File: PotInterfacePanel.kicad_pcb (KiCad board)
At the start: 2 copper layers, 168.1 x 33.4 mm, 29 parts, among them J5 Led, J6 Conn_01x02_Socket, J7 Conn_02x05_Odd_Even, Q1 BC547, Q2 BC547, U1 SM420561N, U2 ATmega328P-P, U4 SM420561N, Y1 Crystal

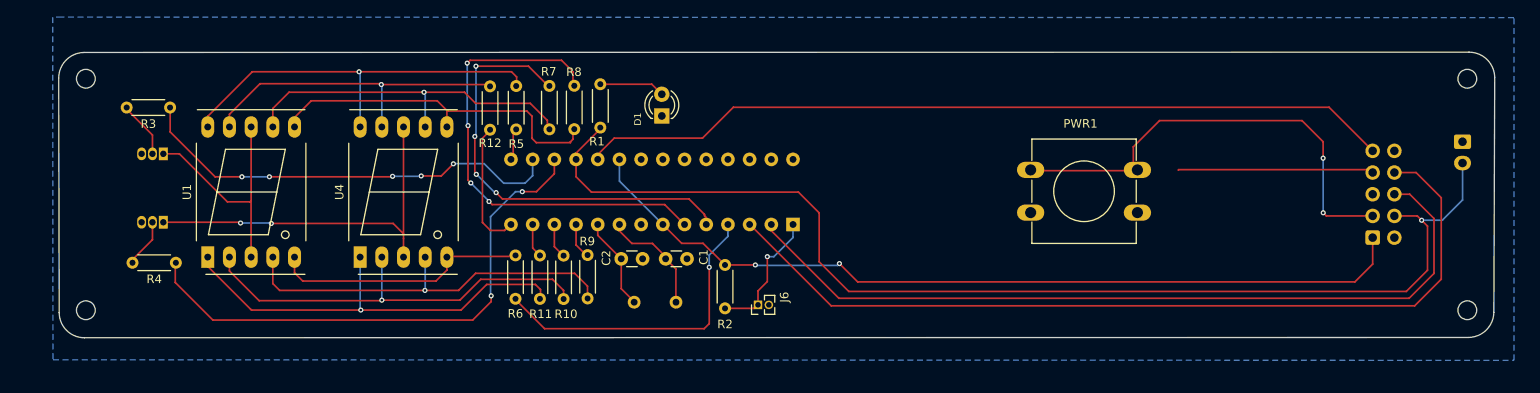
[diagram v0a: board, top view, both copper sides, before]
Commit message: 14seg-Display with a Potentiometer Knob
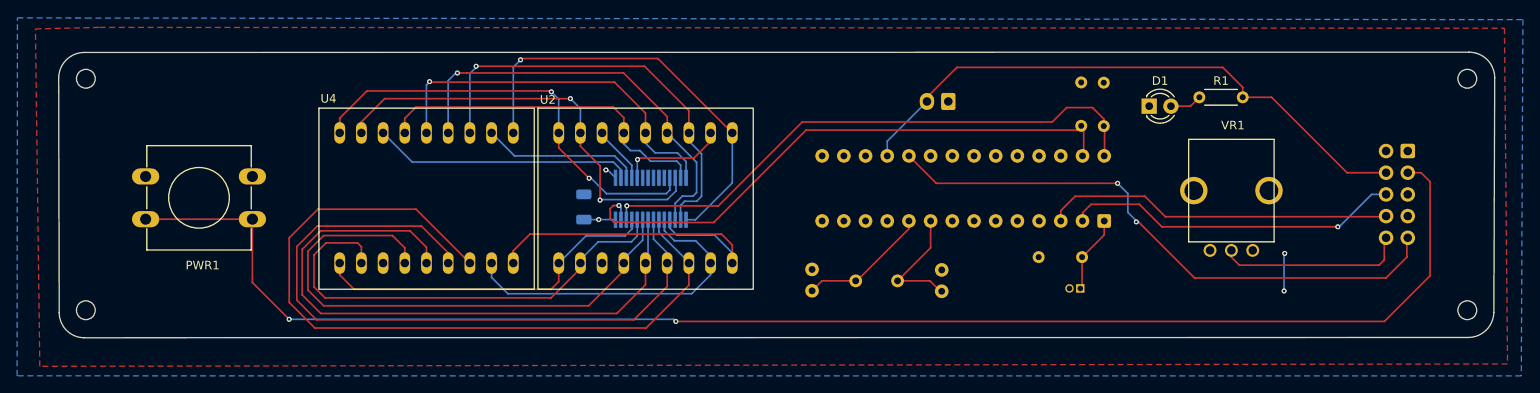
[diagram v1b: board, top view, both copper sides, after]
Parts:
- removed J5: Led, Connector_JST:JST_EH_B2B-EH-A_1x02_P2.50mm_Vertical
- removed J6: Conn_01x02_Socket, Connector_PinHeader_1.27mm:PinHeader_1x02_P1.27mm_Vertical
- removed J7: Conn_02x05_Odd_Even, Connector_IDC:IDC-Header_2x05_P2.54mm_Vertical
- removed Q1, Q2: BC547, Package_TO_SOT_THT:TO-92_Inline
- removed R10, R11, R4, R5, R6, R7, R8, R9: R, Resistor_THT:R_Axial_DIN0204_L3.6mm_D1.6mm_P5.08mm_Horizontal
- added C3: C, Capacitor_SMD:C_1206_3216Metric, B.Cu at (136.3, 95.0)
- added J1: Led, Connector_JST:JST_EH_B2B-EH-A_1x02_P2.50mm_Vertical, B.Cu at (179.0, 82.6)
- added J2: Conn_02x05_Odd_Even, Connector_IDC:IDC-Header_2x05_P2.54mm_Vertical, B.Cu at (232.8, 88.4)
- added J3: Conn_01x02_Socket, Connector_PinHeader_1.27mm:PinHeader_1x02_P1.27mm_Vertical, B.Cu at (194.5, 104.5)
- added U3: ATmega328P-P, Package_DIP:DIP-28_W7.62mm, B.Cu at (197.3, 96.6)
- added VR1: PTV09A-4225F-B104, pot:PTV09, F.Cu at (212.2, 100.1)
- C1, C2: moved to B.Cu
- R12: value R -> 10k; moved to B.Cu
- R2: value 10k -> 4.7k; moved to B.Cu
- R3: value R -> 4.7k; moved to B.Cu
- U1: value SM420561N -> HT16K33A-28SSOP; footprint Display_7Segment:7SegmentLED_LTS6760_LTS6780 -> ht16k33A-28ssop:SOP63P600X175-28N; moved to B.Cu
- U2: value ATmega328P-P -> ~; footprint Package_DIP:DIP-28_W7.62mm -> custom_footprint:14seg; moved to F.Cu
- U4: value SM420561N -> ~; footprint Display_7Segment:7SegmentLED_LTS6760_LTS6780 -> custom_footprint:14seg
- moved R3 106.7 mm to (194.6, 85.5), turned to 90 degrees
- moved PWR1 91.3 mm to (97.5, 96.4), turned to 180 degrees
- moved R1 70.1 mm to (208.4, 82.1), turned to 0 degrees
- moved R12 65.9 mm to (189.6, 100.8), turned to 0 degrees
- moved D1 57.1 mm to (202.5, 83.2), turned to 0 degrees
- moved U1 52.3 mm to (144.2, 94.0), turned to -90 degrees
- moved R2 47.2 mm to (197.2, 85.5), turned to 90 degrees
- moved U2 32.8 mm to (131.0, 83.4), turned to 0 degrees
- moved C1 32.5 mm to (178.2, 104.8), turned to 90 degrees
- moved Y1 26.1 mm to (168.2, 103.6)
- moved C2 22.7 mm to (163.1, 104.8), turned to 90 degrees
- moved U4 18.1 mm to (105.3, 83.4), turned to 0 degrees
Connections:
- C1 pad 1: (no net) -> Net-(U3-XTAL1/PB6)
- C2 pad 1: (no net) -> Net-(U3-XTAL2/PB7)
- D1 pad 2: (no net) -> Net-(D1-A)
- R1 pad 1: (no net) -> Net-(D1-A)
- R12 pad 1: (no net) -> 5V
- R12 pad 2: F -> Net-(J3-Pin_1)
- R2 pad 1: 5V -> /SCL
- R2 pad 2: (no net) -> 5V
- R3 pad 1: (no net) -> /SDA
- R3 pad 2: CC1 -> 5V
- U1 pad 1: E -> GND
- U1 pad 10: G -> unconnected-(U1-ROW15/K13/INT-Pad10)
- U1 pad 2: D -> DG4
- U1 pad 3: (no net) -> DG3
- U1 pad 4: C -> DG2
- U1 pad 5: DPX -> DG1
- U1 pad 6: B -> unconnected-(U1-COM4-Pad6)
- U1 pad 7: A -> unconnected-(U1-COM5-Pad7)
- U1 pad 8: (no net) -> unconnected-(U1-COM6-Pad8)
- U1 pad 9: F -> unconnected-(U1-COM7-Pad9)
- U2 pad 1: (no net) -> e
- U2 pad 10: (no net) -> b
- U2 pad 11: (no net) -> DG1
- U2 pad 12: (no net) -> 1
- U2 pad 13: (no net) -> p
- U2 pad 14: (no net) -> j
- U2 pad 15: (no net) -> h
- U2 pad 16: (no net) -> DG2
- U2 pad 17: (no net) -> g
- U2 pad 18: S. LED -> f
- U2 pad 2: RX -> n
- U2 pad 3: TX -> unconnected-(U2-Pad3)
- U2 pad 4: (no net) -> m
- U2 pad 5: (no net) -> l
- U2 pad 6: (no net) -> k
- U2 pad 7: 5V -> d
- U2 pad 8: GND -> dp
- U2 pad 9: (no net) -> c
- U4 pad 1: E -> e
- U4 pad 10: G -> b
- U4 pad 2: D -> n
- U4 pad 3: (no net) -> unconnected-(U4-Pad3)
- U4 pad 4: C -> m
- U4 pad 5: DPX -> l
- U4 pad 6: B -> k
- U4 pad 7: A -> d
- U4 pad 8: (no net) -> dp
- U4 pad 9: F -> c
- Y1 pad 1: (no net) -> Net-(U3-XTAL2/PB7)
- Y1 pad 2: (no net) -> Net-(U3-XTAL1/PB6)
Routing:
- net (no net): track 410.7 -> 0.00 mm, vias 19 -> 0
- net BT-Pwr: track 55.2 -> 175.8 mm
- net d: track 0.00 -> 91.9 mm
- net 5V: track 99.7 -> 8.36 mm, vias 2 -> 3
- net k: track 0.00 -> 81.9 mm
- net l: track 0.00 -> 73.7 mm
- net /SDA: track 0.00 -> 67.9 mm, vias 0 -> 1
- net /SCL: track 0.00 -> 67.2 mm, vias 0 -> 1
- net S. LED: track 136.2 -> 70.3 mm, vias 1 -> 0
- net m: track 0.00 -> 65.3 mm
- net TX: track 102.5 -> 41.0 mm
- net n: track 0.00 -> 55.9 mm
- net RX: track 95.0 -> 39.6 mm, vias 0 -> 1
- net f: track 0.00 -> 52.9 mm, vias 0 -> 2
- net g: track 0.00 -> 51.1 mm, vias 0 -> 2
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- added copper zone on F.Cu, net 5V
